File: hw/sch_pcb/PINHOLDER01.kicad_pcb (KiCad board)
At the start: 2 copper layers, 26.9 x 50.3 mm, 5 parts, among them J1 HEADER_1x03, M3 HOLE, M4 HOLE

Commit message: Edit PCB
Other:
- rule pad_to_mask_clearance: 0 -> 0.2
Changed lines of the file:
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@@
   )
   (setup
-    (pad_to_mask_clearance 0)
+    (stackup
+      (layer "F.SilkS" (type "Top Silk Screen"))
+      (layer "F.Paste" (type "Top Solder Paste"))
+      (layer "F.Mask" (type "Top Solder Mask") (thickness 0.01))
+      (layer "F.Cu" (type "copper") (thickness 0.035))
+      (layer "dielectric 1" (type "core") (thickness 1.51) (material "FR4") (epsilon_r 4.5) (loss_tangent 0.02))
+      (layer "B.Cu" (type "copper") (thickness 0.035))
+      (layer "B.Mask" (type "Bottom Solder Mask") (thickness 0.01))
+      (layer "B.Paste" (type "Bottom Solder Paste"))
+      (layer "B.SilkS" (type "Bottom Silk Screen"))
+      (copper_finish "None")
+      (dielectric_constraints no)
+    )
+    (pad_to_mask_clearance 0.2)
     (pcbplotparams
       (layerselection 0x00010fc_ffffffff)

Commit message: zamena anoda-katoda
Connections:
- J1 pad 1: Net-(J1-Pad1) -> /circle_0
- J1 pad 3: /circle_0 -> Net-(J1-Pad3)
- TP2 pad 1: Net-(J1-Pad1) -> Net-(J1-Pad3)
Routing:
- net Net-(J1-Pad1): track 9.66 -> 0.00 mm, vias 1 -> 0
- net Net-(J1-Pad3): track 0.00 -> 8.71 mm, vias 0 -> 1
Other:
- board text added: "A"
- board text added: "A GND K"
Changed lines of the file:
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@@
   (net 1 "/circle_0")
   (net 2 "GND")
-  (net 3 "Net-(J1-Pad1)")
+  (net 3 "Net-(J1-Pad3)")
   (footprint "Mlab_Mechanical:MountingHole_3mm" placed (layer "F.Cu")
     (at 114.175179 70.341146)
@@
     (fp_line (start 0 0.5) (end 0 1) (layer "F.Fab") (width 0.15))
     (pad "1" smd rect (at 0 0 180) (size 3.8 2) (layers "F.Cu" "F.Paste" "F.Mask")
-      (net 3 "Net-(J1-Pad1)") (pinfunction "1") (pintype "passive"))
+      (net 3 "Net-(J1-Pad3)") (pinfunction "1") (pintype "passive"))
     (model "${KICAD6_3DMODEL_DIR}/TestPoint.3dshapes/TestPoint_Keystone_5019_Minature.wrl"
       (offset (xyz 0 0 0))
@@
       (effects (font (size 1 1) (thickness 0.15)) (justify mirror))
     )
-    (fp_text value "HEADER_1x03" (at 0 -4.87 90) (layer "B.Fab")
+    (fp_text value "HEADER_1x03" (at 0 -4.87 90) (layer "B.Fab") hide
       (effects (font (size 1 1) (thickness 0.15)) (justify mirror))
     )
@@
     (fp_line (start 2.54 -0.32) (end 1.27 -0.32) (layer "B.Fab") (width 0.1))
     (pad "1" smd rect locked (at -1.655 2.54 90) (size 2.51 1) (layers "B.Cu" "B.Paste" "B.Mask")
-      (net 3 "Net-(J1-Pad1)") (pintype "input"))
+      (net 1 "/circle_0") (pintype "input"))
     (pad "2" smd rect locked (at 1.655 0 90) (size 2.51 1) (layers "B.Cu" "B.Paste" "B.Mask")
       (net 2 "GND") (pintype "input"))
     (pad "3" smd rect locked (at -1.655 -2.54 90) (size 2.51 1) (layers "B.Cu" "B.Paste" "B.Mask")
-      (net 1 "/circle_0") (pintype "input"))
+      (net 3 "Net-(J1-Pad3)") (pintype "input"))
     (model "${KICAD6_3DMODEL_DIR}/Connector_PinHeader_2.54mm.3dshapes/PinHeader_1x03_P2.54mm_Vertical_SMD_Pin1Left.wrl"
       (offset (xyz 0 0 0))
@@
     (effects (font (size 1.7 1.7) (thickness 0.3)) (justify mirror))
   )
+  (gr_text "A GND K" (at 122.1 85.95 180) (layer "B.SilkS")
+    (effects (font (size 1 1) (thickness 0.15)) (justify mirror))
+  )
   (gr_text "PINHOLDER01A" (at 134.08 105.32 90) (layer "F.SilkS")
     (effects (font (size 1.7 1.7) (thickness 0.3)))
   )
-  (via (at 119.7 88.8) (size 0.8) (drill 0.4) (layers "F.Cu" "B.Cu") (net 1))
-  (segment (start 119.7 88.8) (end 119.46 88.56) (width 0.4) (layer "B.Cu") (net 1))
-  (segment (start 119.46 88.56) (end 119.46 83.525) (width 0.4) (layer "B.Cu") (net 1))
-  (segment (start 124.48 76.52) (end 124.11 76.15) (width 0.4) (layer "F.Cu") (net 3))
-  (segment (start 124.11 76.15) (end 122 76.15) (width 0.4) (layer "F.Cu") (net 3))
-  (via (at 124.48 76.52) (size 0.8) (drill 0.4) (layers "F.Cu" "B.Cu") (net 3))
-  (segment (start 124.54 76.58) (end 124.48 76.52) (width 0.4) (layer "B.Cu") (net 3))
-  (segment (start 124.54 83.525) (end 124.54 76.58) (width 0.4) (layer "B.Cu") (net 3))
+  (gr_text "A" (at 122.05 74.05) (layer "F.SilkS")
+    (effects (font (size 1 1) (thickness 0.15)))
+  )
+  (via (at 123.8 88.65) (size 0.8) (drill 0.4) (layers "F.Cu" "B.Cu") (net 1))
+  (segment (start 124.54 87.91) (end 123.8 88.65) (width 0.4) (layer "B.Cu") (net 1))
+  (segment (start 124.54 83.525) (end 124.54 87.91) (width 0.4) (layer "B.Cu") (net 1))
+  (segment (start 120.95 76.55) (end 120.55 76.95) (width 0.4) (layer "F.Cu") (net 3))
+  (segment (start 120.1 76.85) (end 121.3 76.85) (width 0.4) (layer "F.Cu") (net 3))
+  (via (at 120.1 76.85) (size 0.8) (drill 0.4) (layers "F.Cu" "B.Cu") (net 3))
+  (segment (start 120.1 76.85) (end 119.46 77.49) (width 0.4) (layer "B.Cu") (net 3))
+  (segment (start 119.46 77.49) (end 119.46 83.525) (width 0.4) (layer "B.Cu") (net 3))
   (zone (net 1) (net_name "/circle_0") (layer "F.Cu") (name "circle_0") (hatch edge 0.508)
     (priority 10)

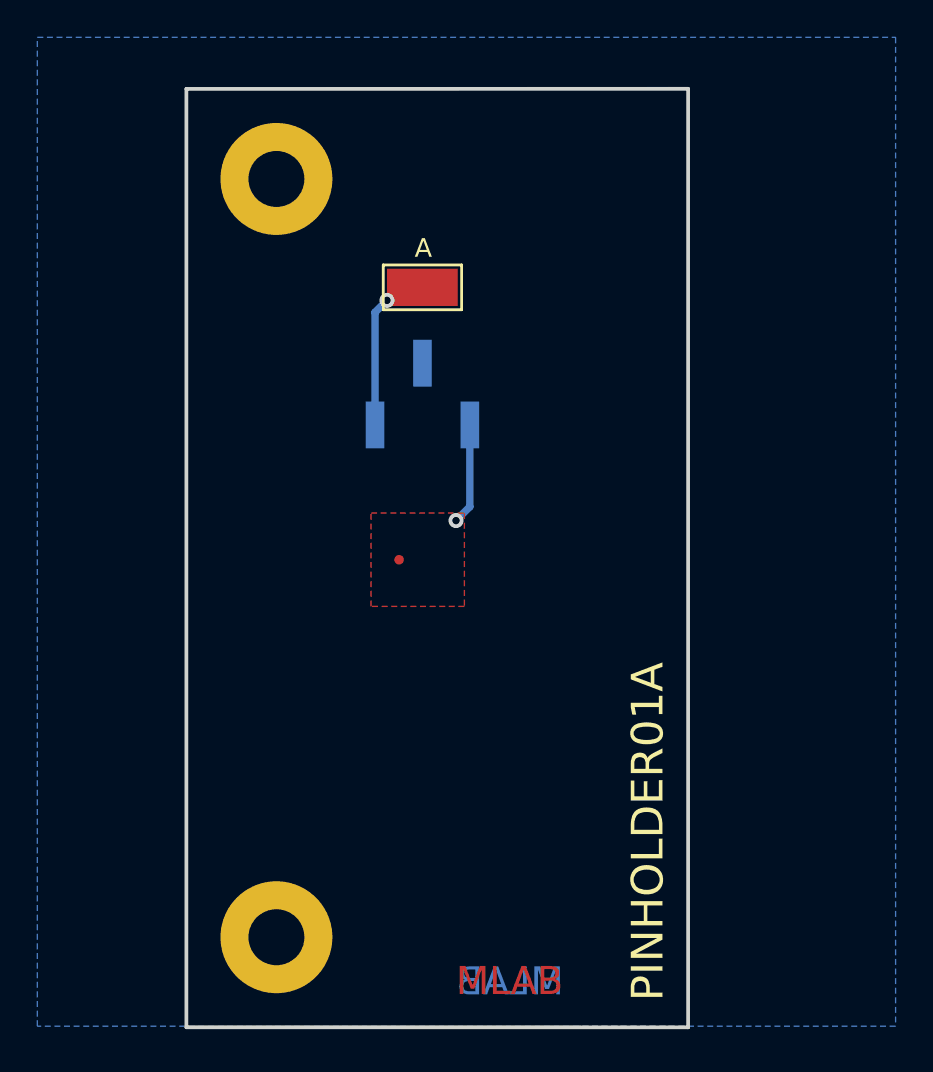
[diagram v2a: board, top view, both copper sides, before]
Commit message: Ortogonal shape Fit to USTSIPIN02A
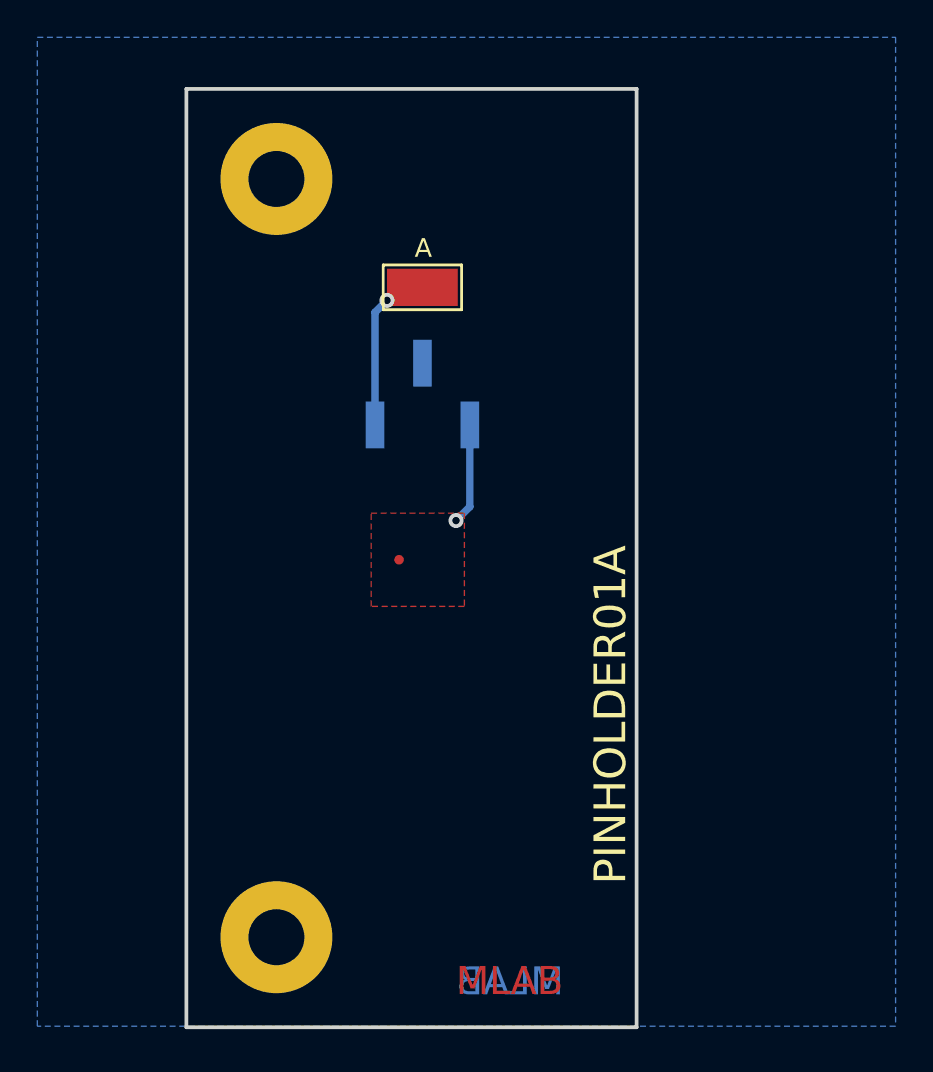
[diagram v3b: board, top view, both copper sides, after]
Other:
- board size 26.9 x 50.3 mm -> 24.1 x 50.3 mm
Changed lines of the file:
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@@
     )
     (pad_to_mask_clearance 0.2)
+    (aux_axis_origin 114.175179 70.341146)
     (pcbplotparams
       (layerselection 0x00010fc_ffffffff)
@@
     )
   )
-  (gr_line (start 136.24 115.81) (end 136.24 65.51) (layer "Edge.Cuts") (width 0.2))
+  (gr_line (start 133.479179 115.807146) (end 133.479179 65.515146) (layer "Edge.Cuts") (width 0.2))
   (gr_line (start 109.349179 115.807146) (end 109.349179 65.515146) (layer "Edge.Cuts") (width 0.2))
-  (gr_line (start 109.349179 115.807146) (end 136.24 115.81) (layer "Edge.Cuts") (width 0.2))
-  (gr_line (start 109.349179 65.515146) (end 136.24 65.51) (layer "Edge.Cuts") (width 0.2))
+  (gr_line (start 109.349179 115.807146) (end 133.479179 115.807146) (layer "Edge.Cuts") (width 0.2))
+  (gr_line (start 109.349179 65.515146) (end 133.479179 65.515146) (layer "Edge.Cuts") (width 0.2))
   (gr_rect (start 134.8 78.6) (end 146.2 90.4) (layer "User.1") (width 0.15) (fill solid))
   (gr_line (start 146.6 78.2) (end 146.6 90.8) (layer "User.2") (width 1))
@@
     (effects (font (size 1.5 1.5) (thickness 0.3)) (justify mirror))
   )
-  (gr_text "PINHOLDER01A" (at 134.4168 105.3592 90) (layer "B.SilkS")
+  (gr_text "PINHOLDER01A" (at 132.08 76.2 90) (layer "B.SilkS")
     (effects (font (size 1.7 1.7) (thickness 0.3)) (justify mirror))
   )
@@
     (effects (font (size 1 1) (thickness 0.15)) (justify mirror))
   )
-  (gr_text "PINHOLDER01A" (at 134.08 105.32 90) (layer "F.SilkS")
+  (gr_text "PINHOLDER01A" (at 132.08 99.06 90) (layer "F.SilkS")
     (effects (font (size 1.7 1.7) (thickness 0.3)))
   )
